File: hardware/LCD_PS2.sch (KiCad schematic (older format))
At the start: 3 parts, among them IC11 LCD-016N002L, X4 KEYBOARD

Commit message: First version of the layout
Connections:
- net GND: now also X4.7
- no-connect marks 3 -> 7
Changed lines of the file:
@@
 L power:GND #PWR?
 U 1 1 5DD59313
-P 5000 5750
+P 5000 5900
 AR Path="/5DD59313" Ref="#PWR?"  Part="1"
 AR Path="/5EB09E21/5DD59313" Ref="#PWR?"  Part="1"
 AR Path="/5DADBF97/5DD59313" Ref="#PWR072"  Part="1"
-F 0 "#PWR072" H 5000 5500 50  0001 C CNN
-F 1 "GND" H 5005 5577 50  0000 C CNN
-F 2 "" H 5000 5750 50  0001 C CNN
-F 3 "" H 5000 5750 50  0001 C CNN
-	1    5000 5750
+F 0 "#PWR072" H 5000 5650 50  0001 C CNN
+F 1 "GND" H 5005 5727 50  0000 C CNN
+F 2 "" H 5000 5900 50  0001 C CNN
+F 3 "" H 5000 5900 50  0001 C CNN
+	1    5000 5900
 	1    0    0    -1
 $EndComp
@@
 	5250 5550 5000 5550
 Wire Wire Line
-	5000 5550 5000 5750
+	5000 5550 5000 5900
 Wire Wire Line
 	5850 5450 5950 5450
@@
 Wire Wire Line
 	5600 2900 5600 3000
+Wire Wire Line
+	5550 5850 5550 5900
+$Comp
+L power:GND #PWR?
+U 1 1 5DA8A71B
+P 5550 5900
+AR Path="/5DA8A71B" Ref="#PWR?"  Part="1"
+AR Path="/5EB09E21/5DA8A71B" Ref="#PWR?"  Part="1"
+AR Path="/5DADBF97/5DA8A71B" Ref="#PWR0102"  Part="1"
+F 0 "#PWR0102" H 5550 5650 50  0001 C CNN
+F 1 "GND" H 5555 5727 50  0000 C CNN
+F 2 "" H 5550 5900 50  0001 C CNN
+F 3 "" H 5550 5900 50  0001 C CNN
+	1    5550 5900
+	1    0    0    -1
+$EndComp
+NoConn ~ 6000 4200
+NoConn ~ 6000 4100
+NoConn ~ 6000 3900
+NoConn ~ 6000 3800
 Wire Bus Line
 	4600 6050 4600 6350

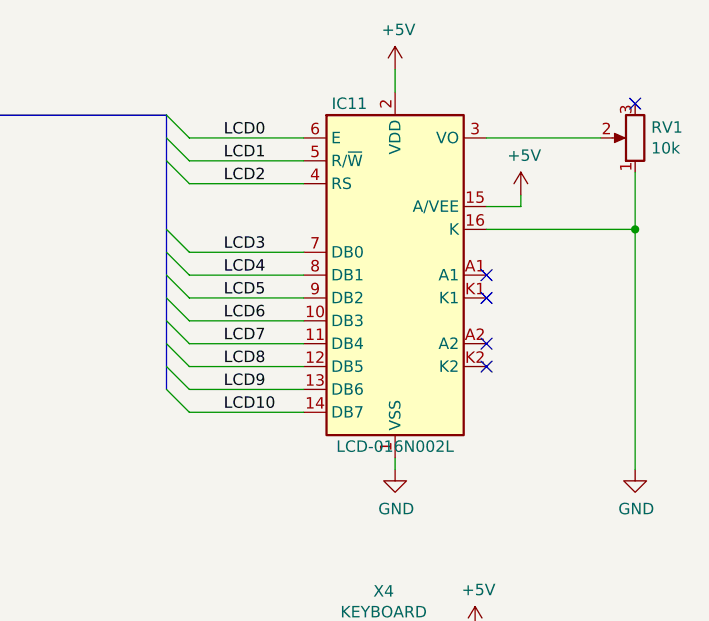
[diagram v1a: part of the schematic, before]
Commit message: Replace LCD
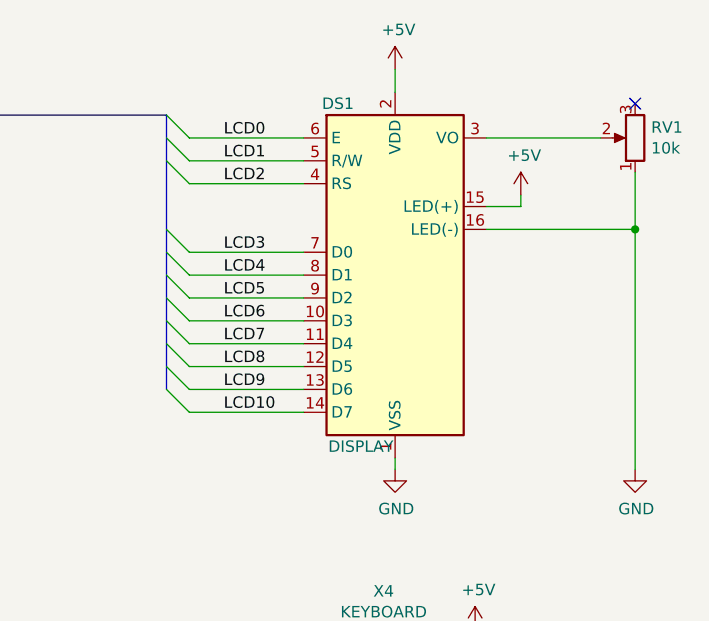
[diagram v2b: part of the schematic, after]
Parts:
- removed IC11: LCD-016N002L, Display:LCD-016N002L, symbol Display_Character:LCD-016N002L
- added DS1: DISPLAY, Display:WC1602A, symbol Display_Character:WC1602A
- RV1: footprint Potentiometer_THT:Potentiometer_Vishay_T73YP_Vertical -> Potentiometer:Bourns_3386T_Vertical; Mfr. Vishay -> Bourns; Mfr. No. T73YP103KT20 -> 3386T-1-103LF; Mouser 72-T73YP103KT20 -> 652-3386T-1-103LF
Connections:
- net +5V: now also DS1.15 (LED(+)), DS1.2 (VDD)
- net GND: now also DS1.1 (VSS), DS1.16 (LED(-))
- net LCD0: now also DS1.6 (E)
- net LCD1: now also DS1.5 (R/W)
- net LCD10: now also DS1.14 (D7)
- net LCD2: now also DS1.4 (RS)
- net LCD3: now also DS1.7 (D0)
- net LCD4: now also DS1.8 (D1)
- net LCD5: now also DS1.9 (D2)
- net LCD6: now also DS1.10 (D3)
- net LCD7: now also DS1.11 (D4)
- net LCD8: now also DS1.12 (D5)
- net LCD9: now also DS1.13 (D6)
- net at RV1.2: now also DS1.3 (VO)
- no-connect marks 7 -> 3
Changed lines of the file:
@@
 	1    0    0    -1
-$EndComp
-$Comp
-L Display_Character:LCD-016N002L IC?
-U 1 1 5DADC5ED
-P 5600 3800
-AR Path="/5EB09E21/5DADC5ED" Ref="IC?"  Part="1"
-AR Path="/5DADBF97/5DADC5ED" Ref="IC11"  Part="1"
-F 0 "IC11" H 5400 4550 50  0000 C CNN
-F 1 "LCD-016N002L" H 5600 3050 50  0000 C CNN
-F 2 "Display:LCD-016N002L" H 5620 2880 50  0001 C CNN
-F 3 "http://www.vishay.com/docs/37299/37299.pdf" H 6100 3500 50  0001 C CNN
-	1    5600 3800
-	1    0    0    -1
-$EndComp
-$Comp
-L Device:R_POT RV1
-U 1 1 5DE99AEE
-P 6650 3200
-F 0 "RV1" H 6580 3154 50  0000 R CNN
-F 1 "10k" H 6580 3245 50  0000 R CNN
-F 2 "Potentiometer_THT:Potentiometer_Vishay_T73YP_Vertical" H 6650 3200 50  0001 C CNN
-F 3 "http://www.vishay.com/docs/51016/t73.pdf" H 6650 3200 50  0001 C CNN
-F 4 "Vishay" H 6650 3200 50  0001 C CNN "Mfr."
-F 5 "T73YP103KT20 " H 6650 3200 50  0001 C CNN "Mfr. No."
-F 6 "72-T73YP103KT20 " H 6650 3200 50  0001 C CNN "Mouser"
-	1    6650 3200
-	-1   0    0    1
 $EndComp
 Entry Wire Line
@@
 	1    0    0    -1
 $EndComp
-NoConn ~ 6000 4200
-NoConn ~ 6000 4100
-NoConn ~ 6000 3900
-NoConn ~ 6000 3800
+$Comp
+L Device:R_POT RV1
+U 1 1 5DE99AEE
+P 6650 3200
+F 0 "RV1" H 6580 3154 50  0000 R CNN
+F 1 "10k" H 6580 3245 50  0000 R CNN
+F 2 "Potentiometer:Bourns_3386T_Vertical" H 6650 3200 50  0001 C CNN
+F 3 "https://www.mouser.de/datasheet/2/54/3386-776606.pdf" H 6650 3200 50  0001 C CNN
+F 4 "Bourns" H 6650 3200 50  0001 C CNN "Mfr."
+F 5 "3386T-1-103LF" H 6650 3200 50  0001 C CNN "Mfr. No."
+F 6 "652-3386T-1-103LF" H 6650 3200 50  0001 C CNN "Mouser"
+	1    6650 3200
+	-1   0    0    1
+$EndComp
 Wire Bus Line
 	4600 6050 4600 6350
 Wire Bus Line
 	4600 3100 4600 4300
+$Comp
+L Display_Character:WC1602A DS1
+U 1 1 5DAA1FEA
+P 5600 3800
+F 0 "DS1" H 5350 4550 50  0000 C CNN
+F 1 "DISPLAY" H 5450 3050 50  0000 C CNN
+F 2 "Display:WC1602A" H 5600 2900 50  0001 C CIN
+F 3 "https://www.mouser.de/datasheet/2/291/NHD-0220GZ-FSW-GBW-L-29740.pdf" H 6300 3800 50  0001 C CNN
+F 4 "Newhaven Display" H 5600 3800 50  0001 C CNN "Mfr."
+F 5 "NHD-0220GZ-FSW-GBW-L" H 5600 3800 50  0001 C CNN "Mfr. No."
+F 6 "763-0220GZ-FSW-GBW" H 5600 3800 50  0001 C CNN "Mouser"
+	1    5600 3800
+	1    0    0    -1
+$EndComp
 $EndSCHEMATC
